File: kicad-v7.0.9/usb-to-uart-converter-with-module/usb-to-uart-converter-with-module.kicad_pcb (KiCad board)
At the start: 2 copper layers, 23.5 x 41.9 mm, 10 parts, among them P1 1x10_pin_header, P2 1x10_pin_header, P3 MLW06A, Q1 MMBT2222, Q2 MMBT2222

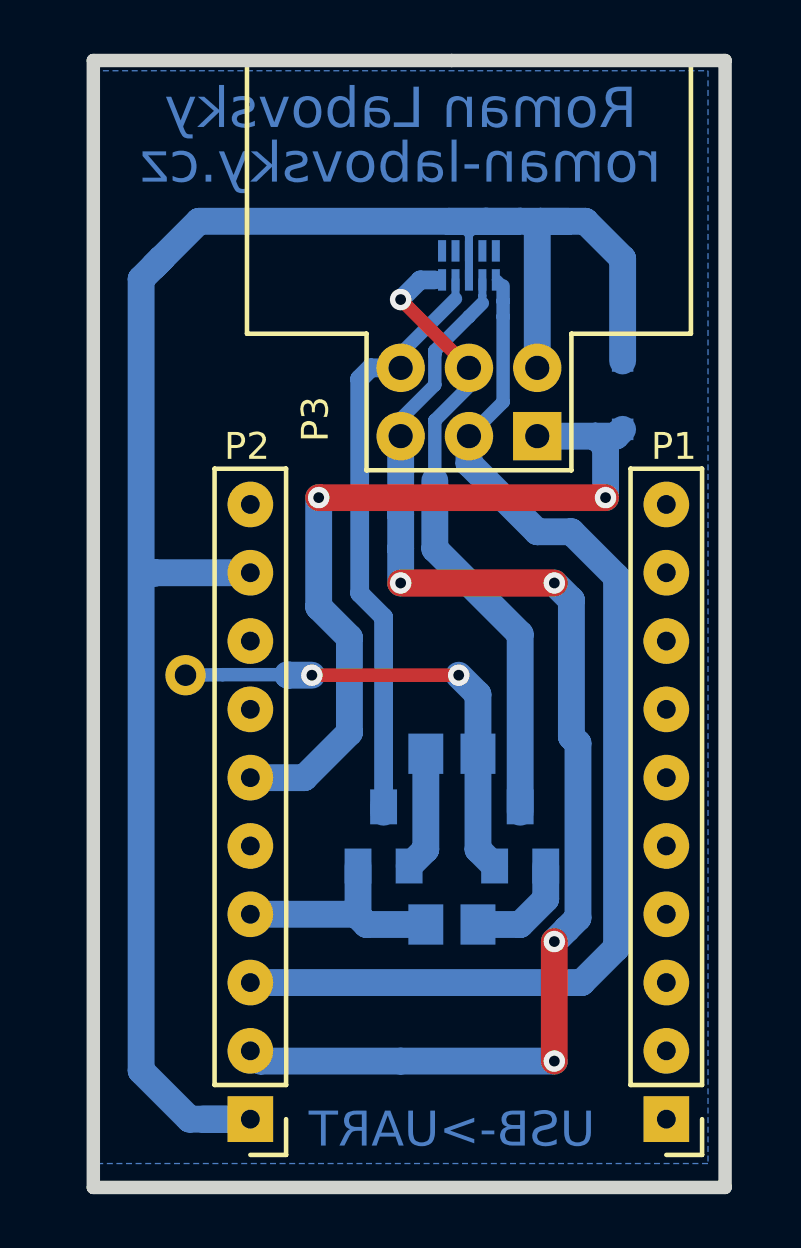
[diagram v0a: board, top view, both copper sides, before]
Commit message: USB to UART converter. Change library. Small changes in schematic a PCB.
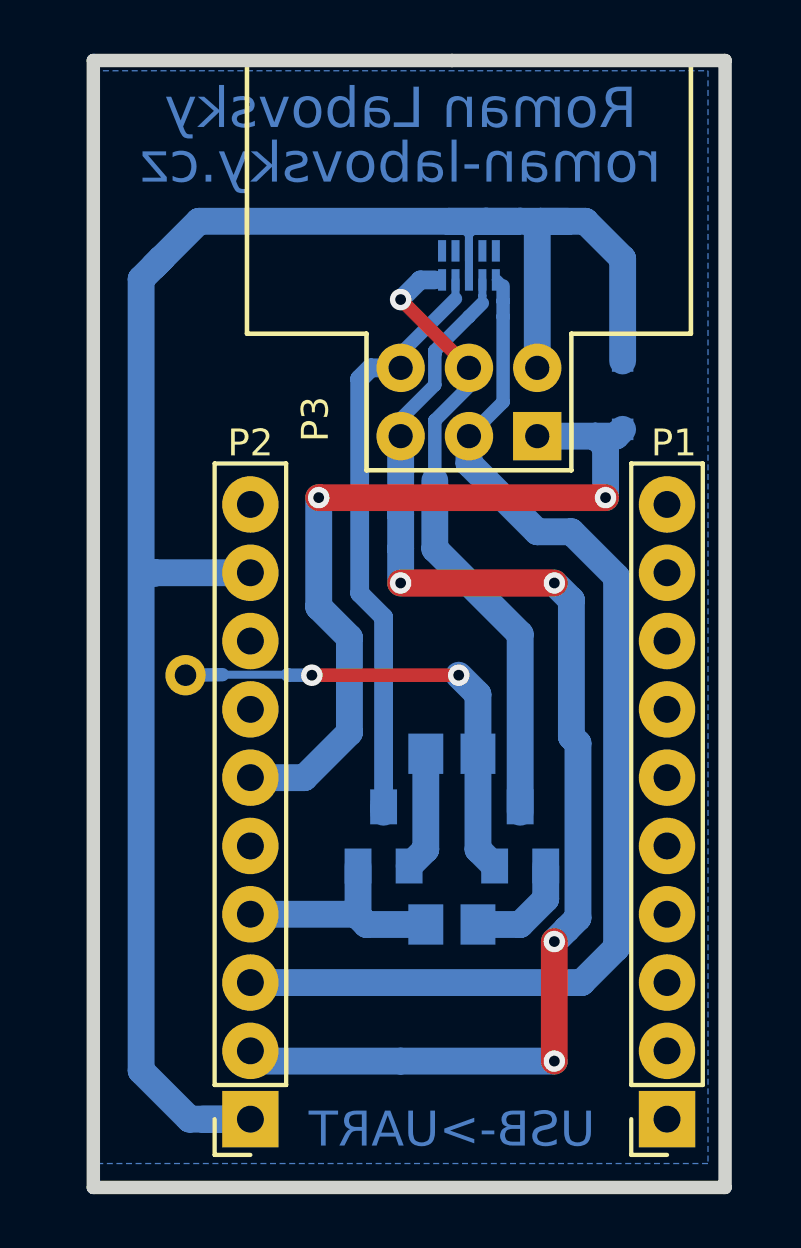
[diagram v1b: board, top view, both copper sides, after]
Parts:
- D1: value SD05.TCT -> SD05-7
- H1: value mounting_hole_pad -> mountig_hole_pad_0.8x1.5mm
- P1, P2: value 1x10_pin_header -> DS1023-1-10S21; footprint connector_rl:1x10_pin_header -> connector_tht_pinsocket_2.54mm_rl:1x10_pinsocket_2.54mm_vertical_8.4mm
- P3: value MLW06A -> 2x3_MLW06A; footprint connector_rl:2x3_pin_header_MLW06A -> connector_idc_rl:2x3_MLW06A
- moved P1 11.4 mm to (95.0, 88.9)
- moved P2 11.4 mm to (79.5, 88.9)

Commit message: Change components form library. Adding of BOM.
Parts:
- P1, P2: footprint connector_tht_pinsocket_2.54mm_rl:1x10_pinsocket_2.54mm_vertical_8.4mm -> connector_pin_socket_2.54mm_tht_rl:1x10_pin_socket_2.54mm_vertical_8.5mm
- P3: footprint connector_idc_rl:2x3_MLW06A -> connector_idc_tht_rl:2x3_MLW06A
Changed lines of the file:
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@@
   (net 27 "Net-(Q1-B)")
   (net 28 "Net-(Q2-B)")
-  (footprint "connector_tht_pinsocket_2.54mm_rl:1x10_pinsocket_2.54mm_vertical_8.4mm" (layer "F.Cu")
+  (footprint "connector_pin_socket_2.54mm_tht_rl:1x10_pin_socket_2.54mm_vertical_8.5mm" (layer "F.Cu")
     (at 94.996 88.9 180)
-    (descr "1x10 pin socket, spacing 2.54 mm, vertical, vertical 8.4 mm")
-    (tags "1x10 pin socket 8.4 mm")
+    (descr "1x10 pin socket, spacing 2.54 mm, vertical, vertical 8.5 mm")
+    (tags "1x10 pin socket 8.5 mm")
     (property "Sheetfile" "usb-to-uart-converter-with-module.kicad_sch")
     (property "Sheetname" "")
@@
     (property "ki_keywords" "1x10 pin socket")
     (attr through_hole)
-    (fp_text reference "P1" (at -0.254 25.146 180) (layer "F.SilkS")
+    (fp_text reference "P1" (at 0 25.146 180) (layer "F.SilkS")
         (effects (font (size 1 1) (thickness 0.15)))
     )
@@
     (pad "10" thru_hole oval (at 0 22.86 180) (size 2.1 2.1) (drill 1) (layers "*.Cu" "*.Mask")
       (net 19 "unconnected-(P1-Pad10)") (pinfunction "10") (pintype "passive+no_connect"))
-    (model "${KICAD_3DPACKAGE_DIR_RL}/connector_pinsocket_2.54mm.3dshapes/tht/1x10_pinsocket_2.54mm_vertical_8.4mm.step"
+    (model "${KICAD_3DPACKAGE_DIR_RL}/connector_pinsocket_2.54mm.3dshapes/tht/1x10_pinsocket_2.54mm_vertical_8.5mm.step"
       (offset (xyz 0 0 0))
       (scale (xyz 1 1 1))
-      (rotate (xyz 0 0 0))
+      (rotate (xyz -90 0 90))
     )
   )
-  (footprint "connector_idc_rl:2x3_MLW06A" (layer "F.Cu")
+  (footprint "connector_idc_tht_rl:2x3_MLW06A" (layer "F.Cu")
     (at 87.63 62.23 90)
     (descr "IDC connector 2x3 MLW06A")
@@
     (property "ki_keywords" "2x3 idc connector MLW06A")
     (attr through_hole)
-    (fp_text reference "P3" (at -0.635 -5.715 90) (layer "F.SilkS")
+    (fp_text reference "P3" (at 1.651 -6.096 180) (layer "F.SilkS")
         (effects (font (size 1 1) (thickness 0.15)))
     )
@@
     )
   )
-  (footprint "connector_tht_pinsocket_2.54mm_rl:1x10_pinsocket_2.54mm_vertical_8.4mm" (layer "F.Cu")
+  (footprint "connector_pin_socket_2.54mm_tht_rl:1x10_pin_socket_2.54mm_vertical_8.5mm" (layer "F.Cu")
     (at 79.502 88.9 180)
-    (descr "1x10 pin socket, spacing 2.54 mm, vertical, vertical 8.4 mm")
-    (tags "1x10 pin socket 8.4 mm")
+    (descr "1x10 pin socket, spacing 2.54 mm, vertical, vertical 8.5 mm")
+    (tags "1x10 pin socket 8.5 mm")
     (property "Sheetfile" "usb-to-uart-converter-with-module.kicad_sch")
     (property "Sheetname" "")
@@
     (property "ki_keywords" "1x10 pin socket")
     (attr through_hole)
-    (fp_text reference "P2" (at 0 25.146 180) (layer "F.SilkS")
+    (fp_text reference "P2" (at 0.127 25.146 180) (layer "F.SilkS")
         (effects (font (size 1 1) (thickness 0.15)))
     )
@@
     (pad "10" thru_hole oval (at 0 22.86 180) (size 2.1 2.1) (drill 1) (layers "*.Cu" "*.Mask")
       (net 26 "unconnected-(P2-Pad10)") (pinfunction "10") (pintype "passive+no_connect"))
-    (model "${KICAD_3DPACKAGE_DIR_RL}/connector_pinsocket_2.54mm.3dshapes/tht/1x10_pinsocket_2.54mm_vertical_8.4mm.step"
+    (model "${KICAD_3DPACKAGE_DIR_RL}/connector_pinsocket_2.54mm.3dshapes/tht/1x10_pinsocket_2.54mm_vertical_8.5mm.step"
       (offset (xyz 0 0 0))
       (scale (xyz 1 1 1))
-      (rotate (xyz 0 0 0))
+      (rotate (xyz -90 0 90))
     )
   )
@@
     (property "ki_description" "ESD protection for ultra high-speed interfaces. Bidirectional protection.")
     (property "ki_keywords" "ESD TVS protection bidirectional")
-    (attr through_hole)
-    (fp_text reference "D2" (at 0 2.794 90) (layer "B.SilkS")
+    (attr smd)
+    (fp_text reference "D2" (at 1.778 0) (layer "B.SilkS")
         (effects (font (size 1 1) (thickness 0.17)) (justify mirror))
     )
-    (fp_text value "PHDMI2AB4Z" (at 0 -2.54 90) (layer "B.Fab")
+    (fp_text value "PHDMI2AB4Z" (at 0 -2.54 270) (layer "B.Fab")
         (effects (font (size 1 1) (thickness 0.15)) (justify mirror))
     )
-    (fp_text user "${REFERENCE}" (at 0 0 180) (layer "B.Fab")
+    (fp_text user "${REFERENCE}" (at 0 0) (layer "B.Fab")
         (effects (font (size 0.55 0.55) (thickness 0.1)) (justify mirror))
     )
